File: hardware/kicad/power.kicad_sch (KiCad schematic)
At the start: 1 part, among them J1 Phoenix_MSTBA_2,5/3-G-5,08

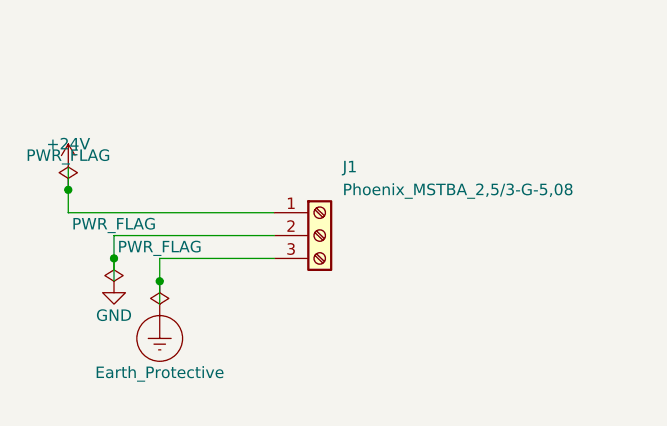
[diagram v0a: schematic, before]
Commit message: kicad: reverse-polarity protection P-MOSFET (Q1) on +24V input
Adds high-side P-MOSFET reverse-polarity protection between
J1 pin 1 and the +24V rail. Q1 (AO3415A, SOT-23, Vds=-40V,
Id=-4A, RDS(on)~70mOhm@-10V) conducts via body diode then
enhances through inverted Vgs when polarity is correct;
under reversed polarity the body diode and channel are both
blocked.

R1 (100k 0603) is the gate-GND pulldown that generates the
negative Vgs needed to turn Q1 on. Vgs at nominal 24V is
well inside the AO3415A +/-25V absolute maximum, so no Vgs
clamp Zener is required.

The +24V power-flag symbol and its PWR_FLAG sentinel move
from J1 pin 1 to Q1 drain - i.e. the "+24V" net name now
refers to the protected rail after Q1, and the raw input
from J1 is unlabeled (local to the J1->Q1.source wire).

Also: nudges +24V/GND/Earth_Protective power-flag positions
one grid step further from their PWR_FLAG sentinels to
remove eeschema text-label overlap (cosmetic; no netlist
change). Verify AO3415A availability on JLCPCB Basic Parts
on order day; fall back to AO3401A (30V Vds) if needed.

ERC passes 0/0. Generation is deterministic.

Co-Authored-By: Claude Opus 4.7 (1M context) <noreply@anthropic.com>
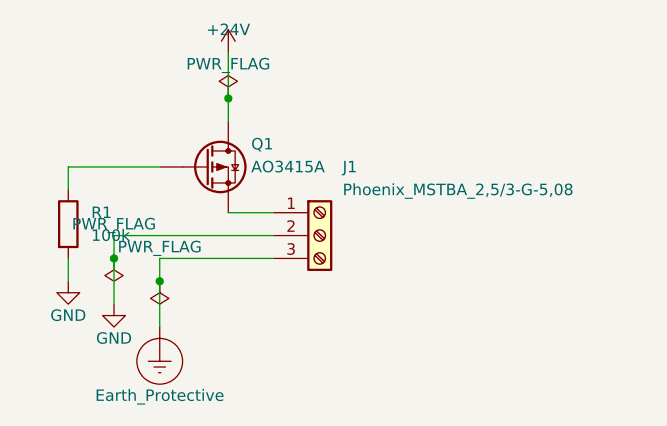
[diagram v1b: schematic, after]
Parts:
- added Q1: AO3415A, symbol Device:Q_PMOS
- added R1: 100k, symbol Device:R
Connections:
- net +24V: now also Q1.D; no longer J1.1 (Pin_1)
- net GND: now also R1.2
- new net: Q1.G, R1.1
- new net: J1.1 (Pin_1), Q1.S
